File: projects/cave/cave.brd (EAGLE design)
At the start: 160 x 100 mm, 111 parts, among them U1 IRLML6344TRPBF, U10 IRLML6344TRPBF, U11 IRLML6344TRPBF, U12 IRLML6344TRPBF, U2 TLC555CDR, U3 IRLML6344TRPBF, U4 IRLML6344TRPBF, U5 IRLML6344TRPBF, U6 IRLML6344TRPBF, U7 TPS54625, U9 IRLML6344TRPBF

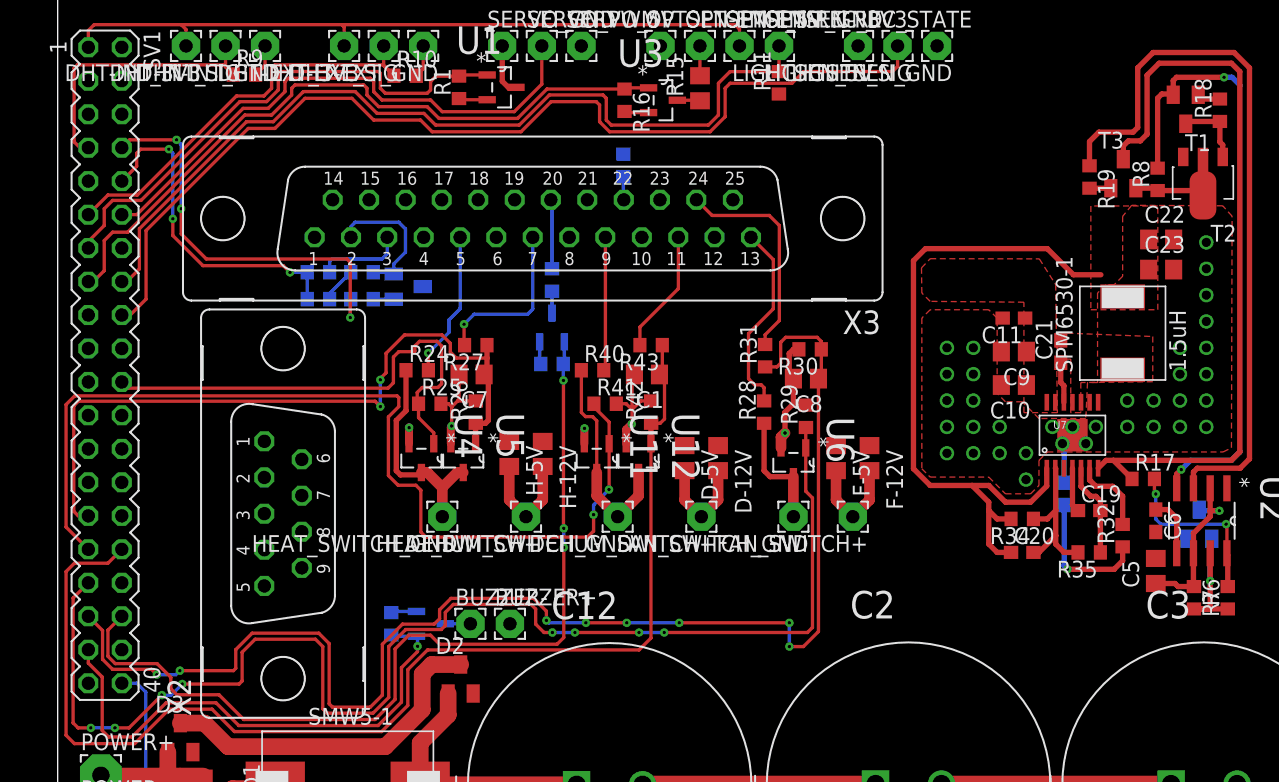
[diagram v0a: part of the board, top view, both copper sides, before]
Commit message: Signal routing done (?), power still to be routed.
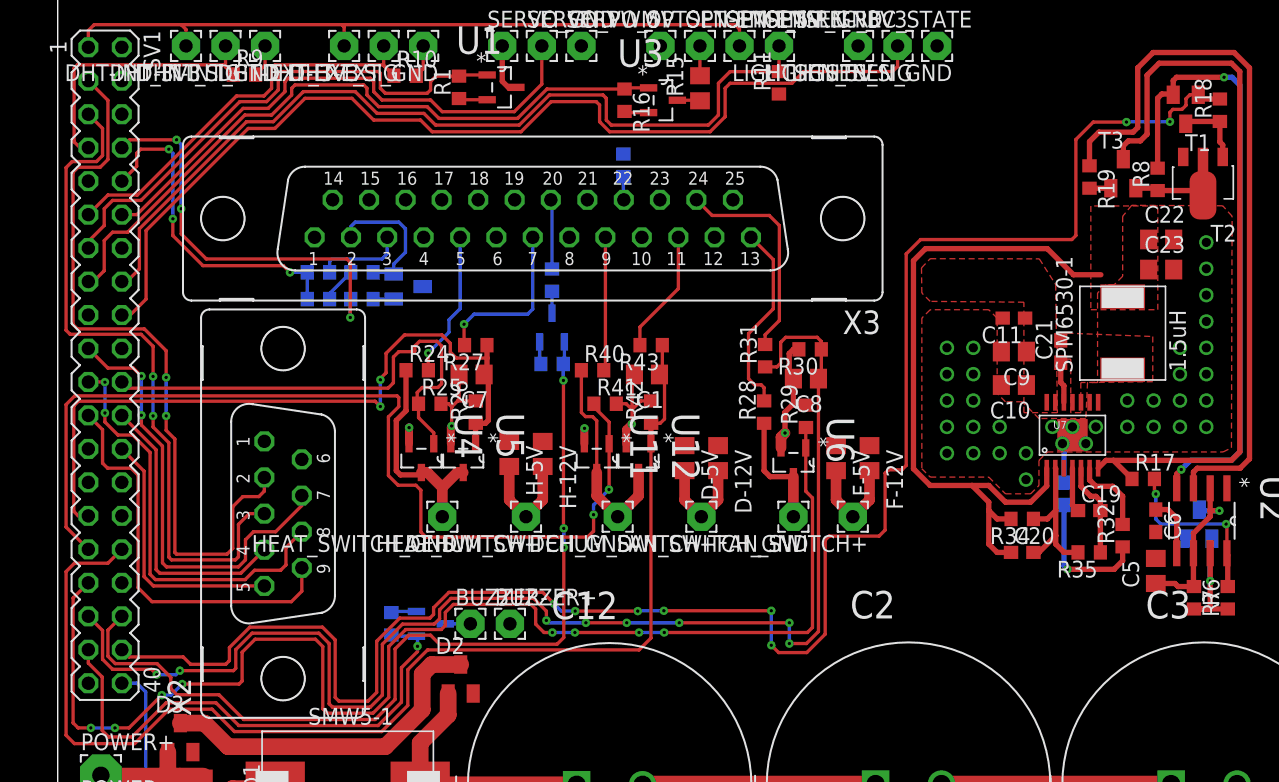
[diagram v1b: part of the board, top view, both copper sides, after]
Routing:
- net WATCHDOG: track 1.78 -> 138.6 mm, vias 0 -> 8
- net I2C_SDA: track 0.00 -> 56.4 mm, vias 0 -> 2
- net I2C_SCL: track 0.00 -> 52.9 mm, vias 0 -> 2
- net SPI_MOSI: track 0.00 -> 34.0 mm, vias 0 -> 2
- net SPI_MISO: track 0.00 -> 31.9 mm, vias 0 -> 2
- net SPI_SCLK: track 0.00 -> 30.6 mm
- net SPI_CE0: track 0.00 -> 21.8 mm
- net SPI_CE1: track 0.00 -> 19.8 mm

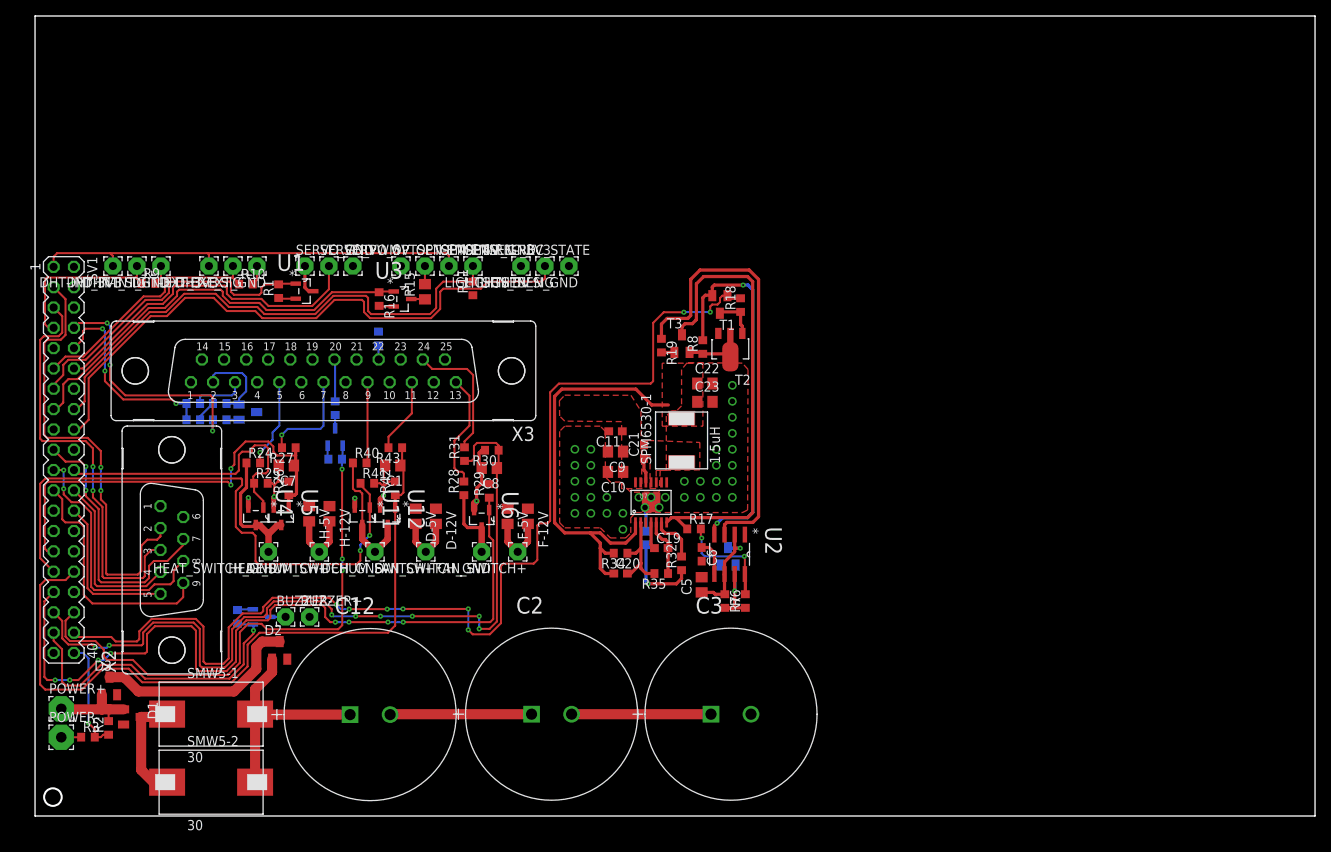
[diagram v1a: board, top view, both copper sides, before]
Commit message: Routing done !! Changed 5V to +5V on 25-pin Sub-D. Modified Routing_prefs script.
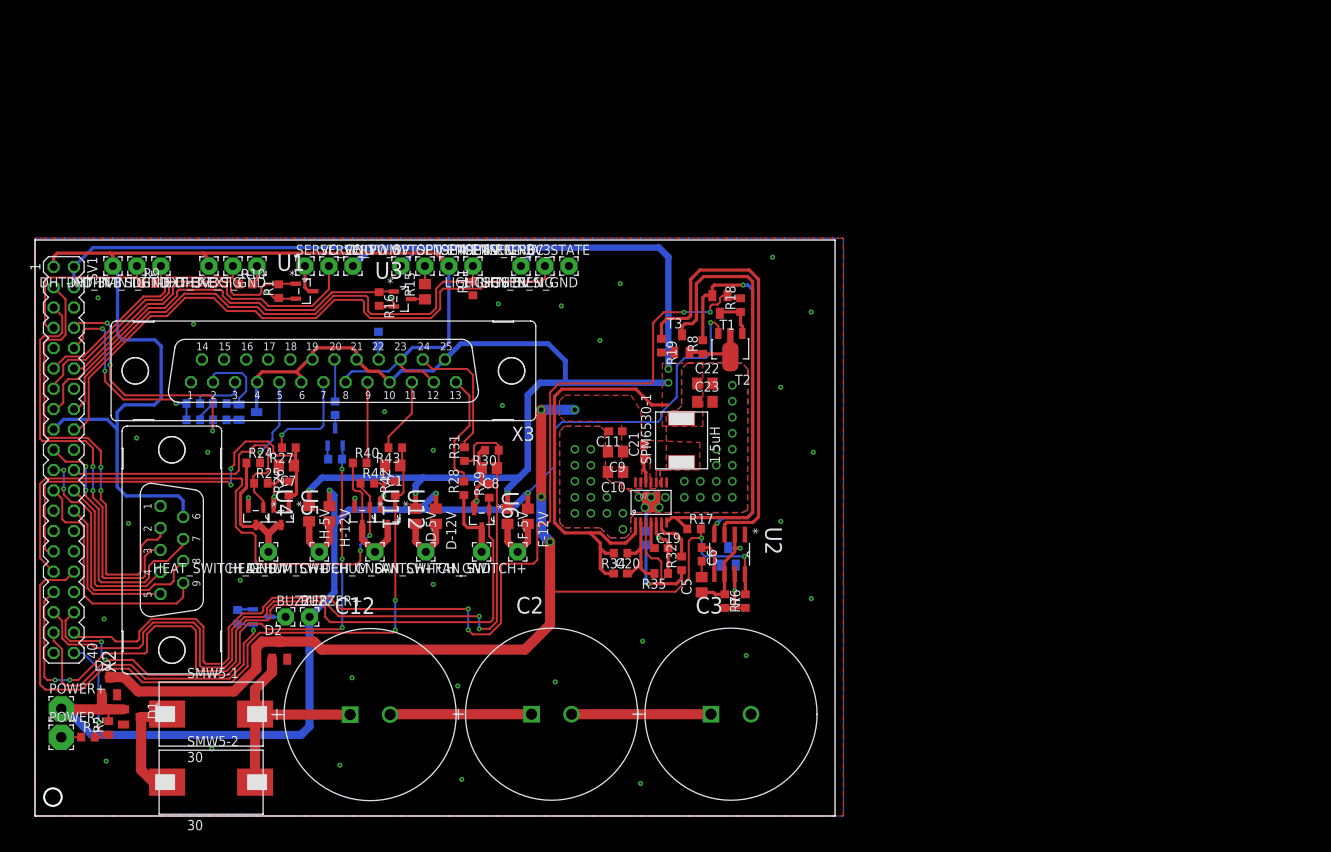
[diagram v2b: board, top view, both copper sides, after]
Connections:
- removed net 5V: SV1.4, X3.10, X3.19, X3.21, X3.25, X3.4, X3.6
- net +5V: now also SV1.4, X3.10, X3.19, X3.21, X3.25, X3.4, X3.6
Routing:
- net +5V: track 53.1 -> 278.5 mm, vias 0 -> 5
- net +12V: track 11.1 -> 150.9 mm, vias 0 -> 4
- net VCOND: track 39.6 -> 131.1 mm, vias 2 -> 6
- net +3V3: track 55.7 -> 142.8 mm
- net N$28: track 10.5 -> 19.4 mm
- net GND: track 62.1 -> 66.9 mm, vias 40 -> 74
- net POWER_STATE: track 14.1 -> 14.9 mm
- net LED_RUN: track 68.4 -> 69.2 mm, vias 3 -> 5
- net FAN_LEVER_F: track 103.2 -> 102.9 mm, vias 8 -> 2
- net DEHUM_LEVER_F: track 91.6 -> 92.0 mm, vias 0 -> 2
- net WATCHDOG: vias 8 -> 4
- net FAN_SWITCH: vias 8 -> 2
- added copper zone on layer 16, net GND
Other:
- board size 160 x 100 mm -> 100 x 72 mm

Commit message: Added fixing holes for M2 screws (2.2mm vias). Rounded corners.
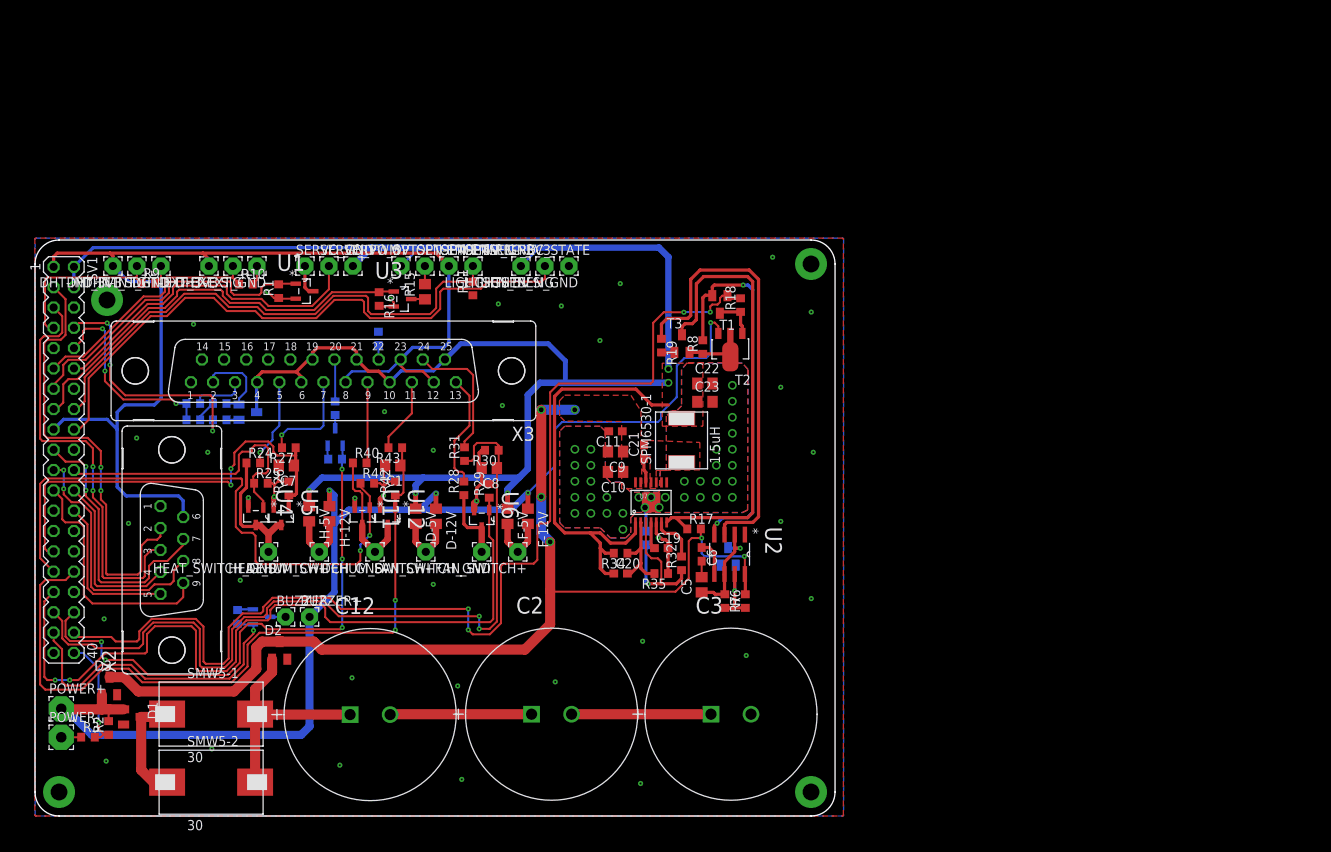
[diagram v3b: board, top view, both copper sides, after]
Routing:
- net GND: vias 74 -> 73
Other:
- outline, holes or cut-outs redrawn
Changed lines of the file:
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@@
 <setting verticaltext="up"/>
 </settings>
-<grid distance="10" unitdist="mil" unit="mm" style="lines" multiple="1" display="yes" altdistance="10" altunitdist="mil" altunit="mil"/>
+<grid distance="0.5" unitdist="mm" unit="mm" style="lines" multiple="1" display="yes" altdistance="10" altunitdist="mil" altunit="mil"/>
 <layers>
 <layer number="1" name="Top" color="4" fill="1" visible="yes" active="yes"/>
@@
 <board>
 <plain>
-<wire x1="0" y1="0" x2="100" y2="0" width="0" layer="20"/>
-<wire x1="100" y1="0" x2="100" y2="72" width="0" layer="20"/>
-<wire x1="100" y1="72" x2="0" y2="72" width="0" layer="20"/>
-<wire x1="0" y1="72" x2="0" y2="0" width="0" layer="20"/>
-<circle x="2.2352" y="2.3622" radius="1.1" width="0.254" layer="20"/>
+<wire x1="0" y1="69" x2="0" y2="3" width="0" layer="20"/>
+<wire x1="0" y1="3" x2="3" y2="0" width="0" layer="20" curve="90"/>
+<wire x1="3" y1="0" x2="97" y2="0" width="0" layer="20"/>
+<wire x1="97" y1="0" x2="100" y2="3" width="0" layer="20" curve="90"/>
+<wire x1="100" y1="3" x2="100" y2="69" width="0" layer="20"/>
+<wire x1="100" y1="69" x2="97" y2="72" width="0" layer="20" curve="90"/>
+<wire x1="97" y1="72" x2="3" y2="72" width="0" layer="20"/>
+<wire x1="3" y1="72" x2="0" y2="69" width="0" layer="20" curve="90"/>
 </plain>
 <attributes>
@@
 <via x="58.42" y="51.308" extent="1-16" drill="0.25"/>
 <via x="19.812" y="61.468" extent="1-16" drill="0.25"/>
-<via x="7.874" y="64.77" extent="1-16" drill="0.25"/>
 <via x="12.7" y="47.244" extent="1-16" drill="0.25"/>
 <via x="21.59" y="45.466" extent="1-16" drill="0.25"/>
@@
 <wire x1="11.176" y1="51.3842" x2="14.9352" y2="51.3842" width="0.4064" layer="16"/>
 <wire x1="14.9352" y1="51.3842" x2="15.7734" y2="52.2224" width="0.4064" layer="16"/>
-<wire x1="15.7734" y1="52.2224" x2="15.7734" y2="58.7248" width="0.4064" layer="16"/>
-<wire x1="15.7734" y1="58.7248" x2="14.986" y2="59.5122" width="0.4064" layer="16"/>
-<wire x1="14.986" y1="59.5122" x2="10.9982" y2="59.5122" width="0.4064" layer="16"/>
-<wire x1="10.9982" y1="59.5122" x2="10.3124" y2="60.198" width="0.4064" layer="16"/>
-<wire x1="10.3124" y1="60.198" x2="10.3124" y2="68.1702" width="0.4064" layer="16"/>
-<wire x1="10.3124" y1="68.1702" x2="9.7366" y2="68.746" width="0.4064" layer="16"/>
+<wire x1="15.7734" y1="52.2224" x2="15.7734" y2="66.0146" width="0.4064" layer="16"/>
+<wire x1="15.7734" y1="66.0146" x2="14.986" y2="66.802" width="0.4064" layer="16"/>
+<wire x1="14.986" y1="66.802" x2="11.6806" y2="66.802" width="0.4064" layer="16"/>
+<wire x1="11.6806" y1="66.802" x2="9.7366" y2="68.746" width="0.4064" layer="16"/>
 </signal>
 <signal name="I2C_SDA">
@@
 <signal name="N$39">
 </signal>
+<signal name="N$8">
+<via x="3" y="3" extent="1-16" drill="2.1" diameter="4"/>
+</signal>
+<signal name="N$18">
+<via x="97" y="3" extent="1-16" drill="2.1" diameter="4"/>
+</signal>
+<signal name="N$19">
+<via x="97" y="69" extent="1-16" drill="2.1" diameter="4"/>
+</signal>
+<signal name="N$29">
+<via x="9" y="64.5" extent="1-16" drill="2.1" diameter="4"/>
+</signal>
 </signals>
